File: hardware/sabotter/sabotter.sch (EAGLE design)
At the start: 112 parts, among them IC1 MAX3232CSE, IC2 MAX3232CSE, IC3 OKI-78SR-3.3/1.5-W36H-C, IC4 OKI-78SR-5/1.5-W36H-C, IC6 ATXMEGA256A3U-AU, IC7 LM4871M, T1 2n2222, T2 2n2222, T3 2n2222

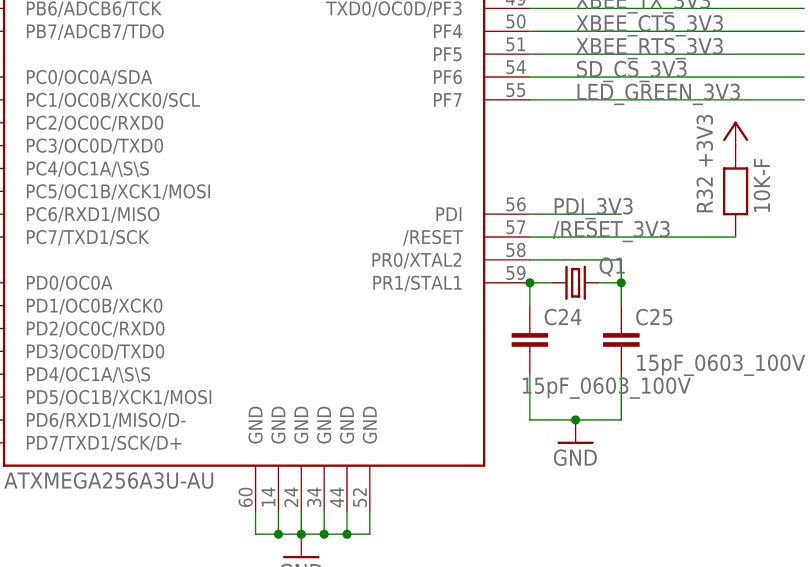
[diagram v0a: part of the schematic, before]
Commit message: milling deleted on some connectors
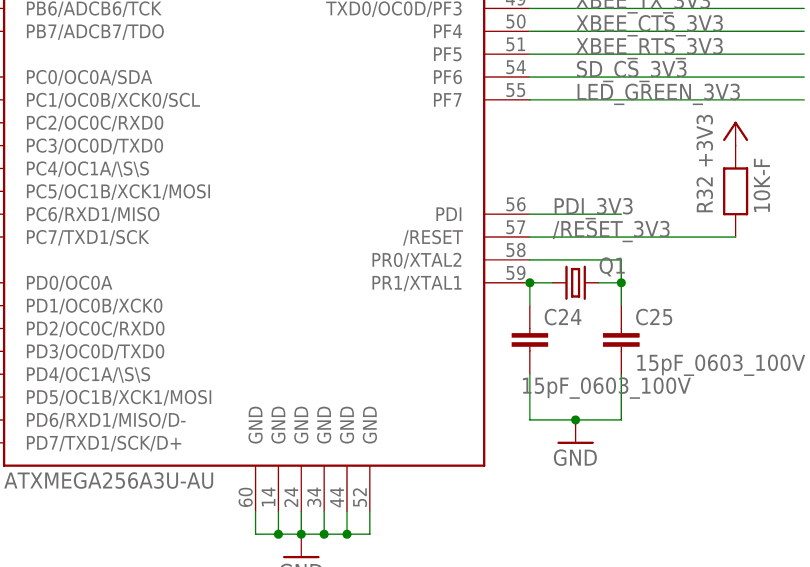
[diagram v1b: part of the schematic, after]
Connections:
- net N$75: now also IC6.PR1/XTAL1; no longer IC6.PR1/STAL1
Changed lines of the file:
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@@
 <segment>
 <pinref part="C24" gate="G$1" pin="1"/>
-<pinref part="IC6" gate="G$1" pin="PR1/STAL1"/>
+<pinref part="IC6" gate="G$1" pin="PR1/XTAL1"/>
 <wire x1="121.92" y1="60.96" x2="121.92" y2="63.5" width="0.1524" layer="91"/>
 <pinref part="Q1" gate="G$1" pin="1"/>

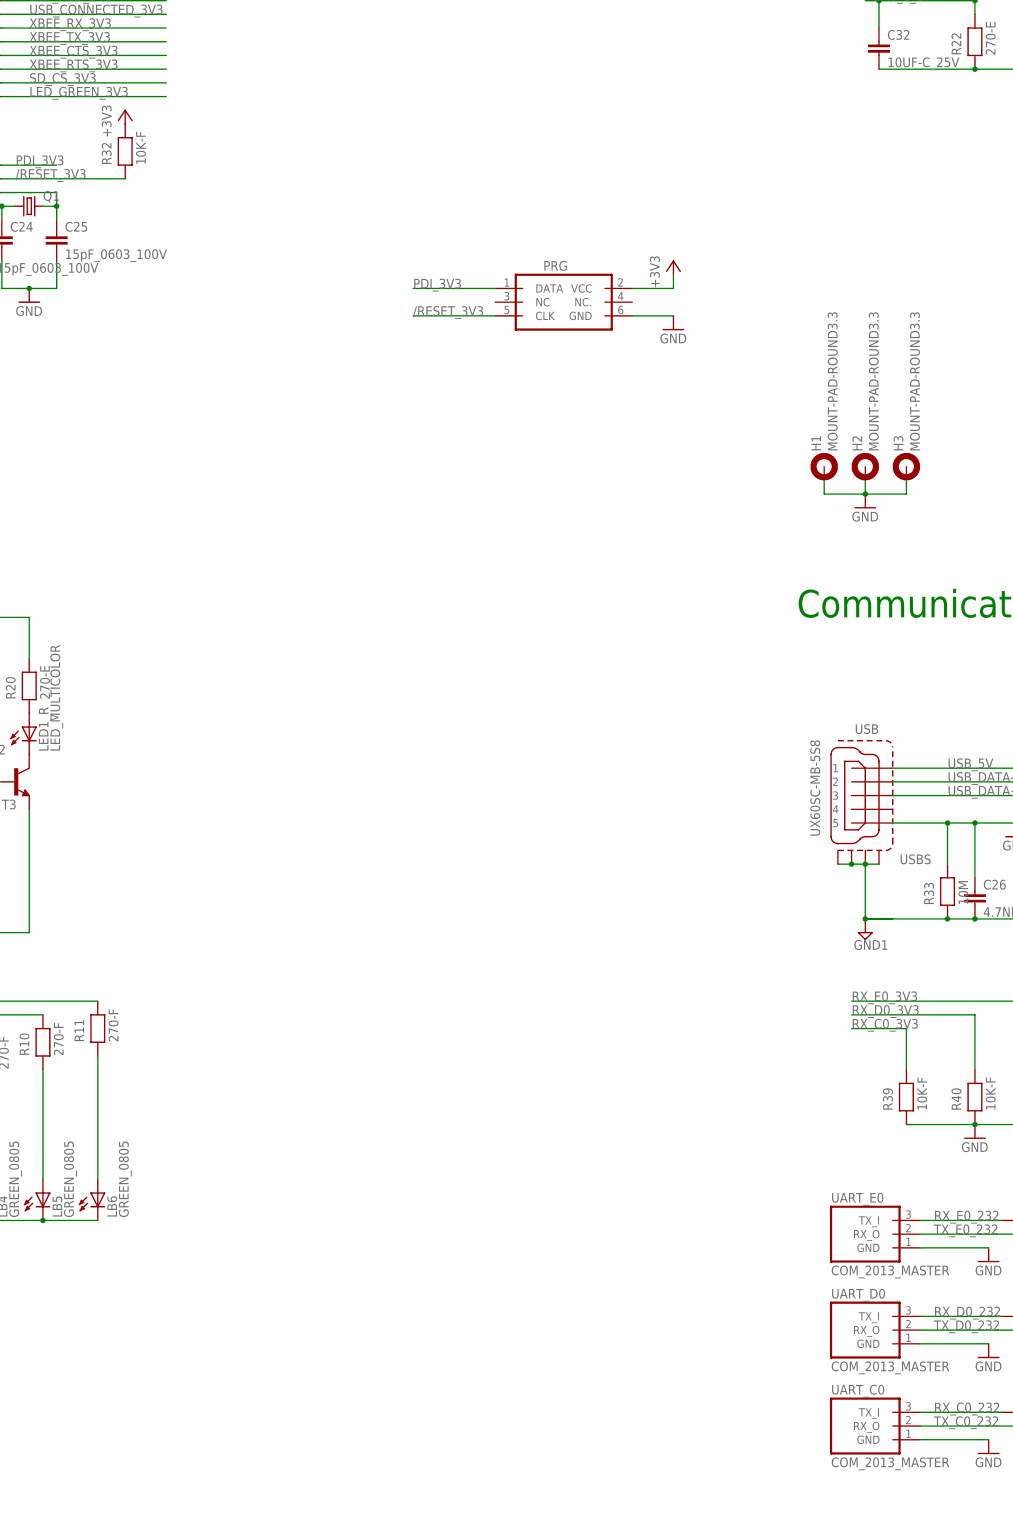
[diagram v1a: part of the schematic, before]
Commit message: mouser component ref added
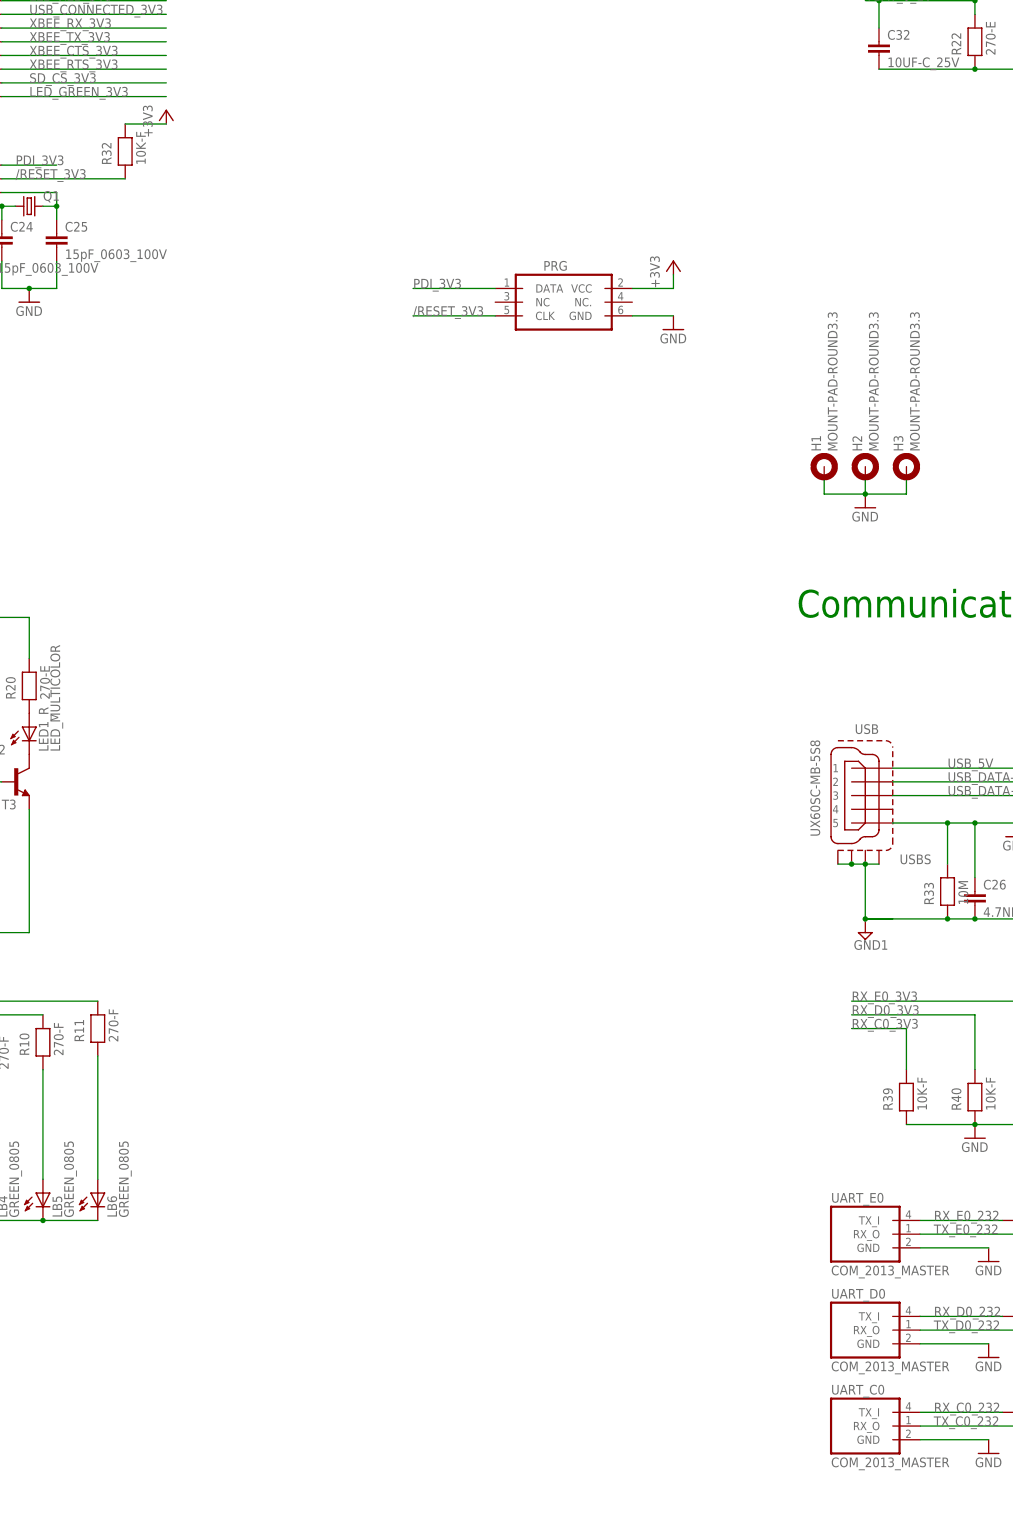
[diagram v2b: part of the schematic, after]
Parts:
- BAT: device con-molex:22-27-2021-02 -> robotter_connector:22-27-2021-02
- T1, T2, T3: device transistor-neu-to92:MMBT2222ALT1-NPN-SOT23-BEC -> robotter_ic:MMBT2222ALT1-NPN-SOT23-BEC
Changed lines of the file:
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@@
 <part name="GND24" library="supply1" deviceset="GND" device=""/>
 <part name="D1" library="robotter_diode" deviceset="MBRA340T3" device=""/>
-<part name="T1" library="transistor-neu-to92" deviceset="*-NPN-" device="SOT23-BEC" technology="MMBT2222ALT1" value="2n2222"/>
-<part name="T2" library="transistor-neu-to92" deviceset="*-NPN-" device="SOT23-BEC" technology="MMBT2222ALT1" value="2n2222"/>
-<part name="T3" library="transistor-neu-to92" deviceset="*-NPN-" device="SOT23-BEC" technology="MMBT2222ALT1" value="2n2222"/>
+<part name="T1" library="robotter_ic" deviceset="*-NPN-" device="SOT23-BEC" technology="MMBT2222ALT1" value="2n2222"/>
+<part name="T2" library="robotter_ic" deviceset="*-NPN-" device="SOT23-BEC" technology="MMBT2222ALT1" value="2n2222"/>
+<part name="T3" library="robotter_ic" deviceset="*-NPN-" device="SOT23-BEC" technology="MMBT2222ALT1" value="2n2222"/>
 <part name="R12" library="robotter_resistor" deviceset="1K" device="-F"/>
 <part name="R13" library="robotter_resistor" deviceset="1K" device="-F"/>
@@
 <part name="C22" library="robotter_capacitor" deviceset="100NF" device="-F" value="100nF_0603_50V"/>
 <part name="C23" library="robotter_capacitor" deviceset="100NF" device="-F" value="100nF_0603_50V"/>
-<part name="L1" library="robotter_inductor" deviceset="FERRITE_" device="220OHMS"/>
+<part name="L1" library="robotter_inductor" deviceset="FERRITE_220OHMS" device=""/>
 <part name="+3V8" library="supply1" deviceset="+3V3" device=""/>
 <part name="GND9" library="supply1" deviceset="GND" device=""/>
@@
 <part name="GND19" library="supply1" deviceset="GND" device=""/>
 <part name="R34" library="robotter_resistor" deviceset="10K" device="-F"/>
-<part name="BAT" library="con-molex" deviceset="22-?-02" device="27-2021"/>
+<part name="BAT" library="robotter_connector" deviceset="22-?-02" device="27-2021"/>
 <part name="COLOR/START" library="robotter_connector" deviceset="794618-4" device=""/>
 <part name="GND14" library="supply1" deviceset="GND" device=""/>
@@
 </instance>
 <instance part="R32" gate="G$1" x="144.78" y="73.66" rot="R90"/>
-<instance part="+3V9" gate="G$1" x="144.78" y="81.28"/>
+<instance part="+3V9" gate="G$1" x="152.4" y="81.28"/>
 <instance part="GND26" gate="1" x="127" y="45.72"/>
 <instance part="PRG" gate="1" x="226.06" y="45.72"/>
@@
 <pinref part="R32" gate="G$1" pin="2"/>
 <pinref part="+3V9" gate="G$1" pin="+3V3"/>
-</segment>
-<segment>
+<wire x1="152.4" y1="78.74" x2="144.78" y2="78.74" width="0.1524" layer="91"/>
+</segment>
+<segment>
